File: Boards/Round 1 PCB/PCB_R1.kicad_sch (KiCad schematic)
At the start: 67 parts, among them J1 Screw_Terminal_01x12, J10 Screw_Terminal_01x03, J11 Screw_Terminal_01x12, J12 Screw_Terminal_01x03, J13 Screw_Terminal_01x03, J14 Screw_Terminal_01x03, J15 Screw_Terminal_01x03, J16 Screw_Terminal_01x03, J17 Screw_Terminal_01x03, J18 Screw_Terminal_01x03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

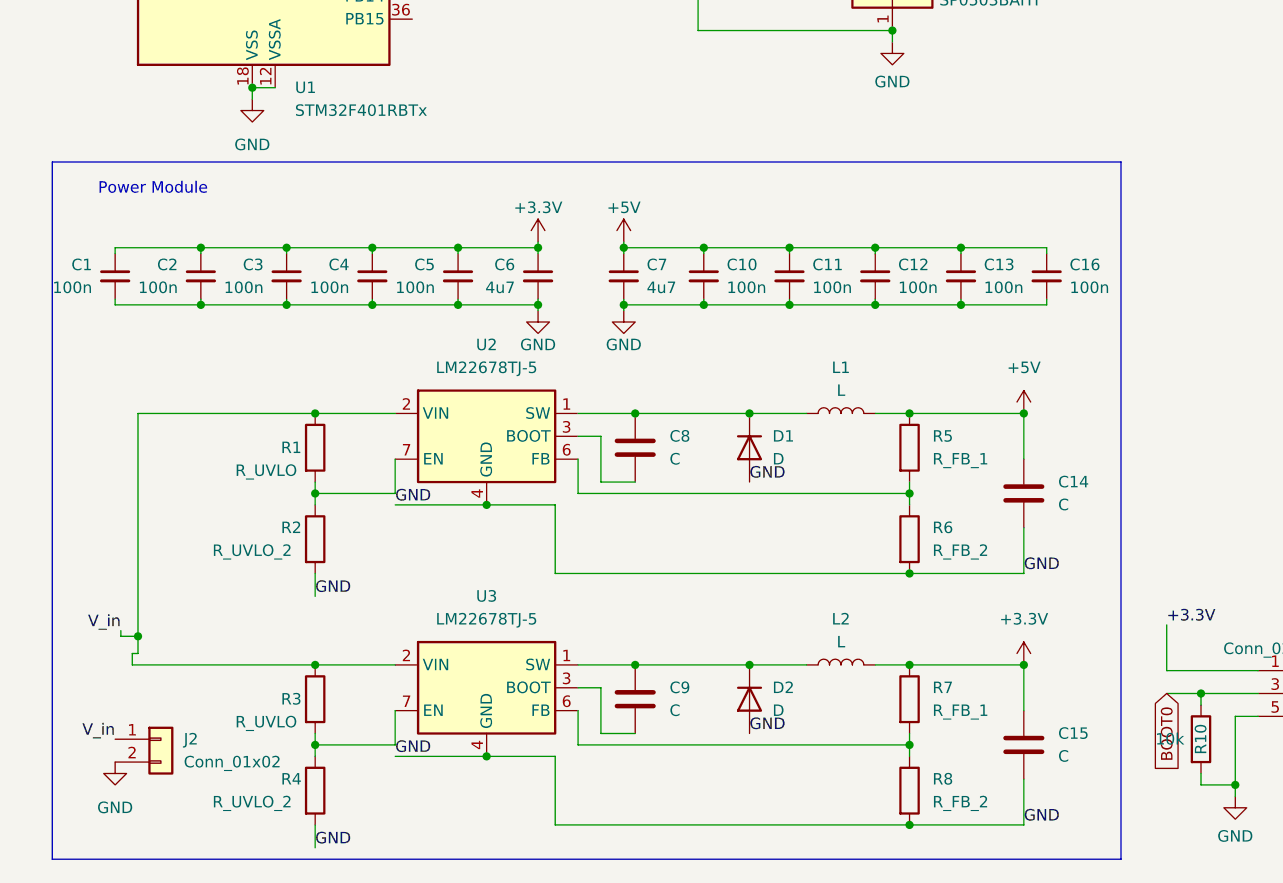
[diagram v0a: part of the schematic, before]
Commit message: Power System Update
added component values to the power system, and fixed ground nets
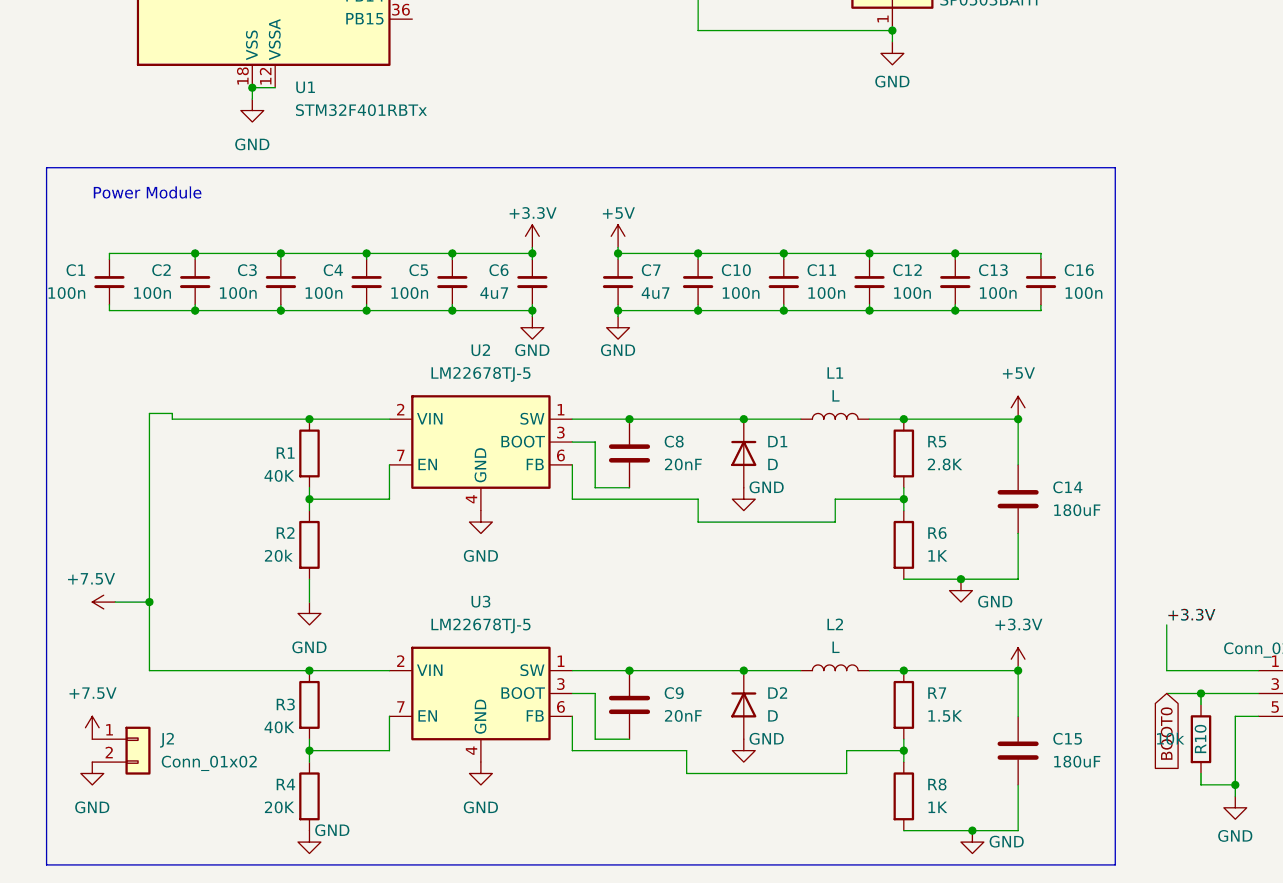
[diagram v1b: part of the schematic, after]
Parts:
- C14, C15: value C -> 180uF
- C8, C9: value C -> 20nF
- R1, R3: value R_UVLO -> 40K
- R2: value R_UVLO_2 -> 20k
- R4: value R_UVLO_2 -> 20K
- R5: value R_FB_1 -> 2.8K
- R6, R8: value R_FB_2 -> 1K
- R7: value R_FB_1 -> 1.5K
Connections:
- net V_in renamed +7.5V
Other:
- moved on the sheet: C1, C10, C11, C12, C13, C14, C15, C16, C2, C3, C4, C5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

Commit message: Inductor update
oops, I forgot the inductor values again
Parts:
- L1: value L -> 60uH
- L2: value L -> 2.2uH
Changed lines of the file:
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@@
       (effects (font (size 1.27 1.27)))
     )
-    (property "Value" "L" (at 100.33 172.72 90)
+    (property "Value" "2.2uH" (at 100.33 172.72 90)
       (effects (font (size 1.27 1.27)))
     )
@@
       (effects (font (size 1.27 1.27)))
     )
-    (property "Value" "L" (at 100.33 144.78 90)
-      (effects (font (size 1.27 1.27)))
-    )
+    (property "Value" "60uH" (at 100.33 144.78 90)
+      (effects (font (size 1.27 1.27)))
+    )

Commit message: Misc updates from 3/17/24
Touched up a few really minor things while I was doing the parts list
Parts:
- C17: value C -> 2.2uF
- D3: value SP0503BAHT -> SP0503BAHTG
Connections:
- net 3.3V_OUT is gone; now on net +3.3V: U1.13 (VREF+)
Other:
- note removed: "Gyroscope and Acceleromiter"

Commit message: r1 SMD footprint updates
changed component footprints on the board and schematic to use free smd components
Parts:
- C1, C10, C11, C12, C13, C16, C2, C3, C4, C5: footprint Capacitor_SMD:C_0402_1005Metric -> Capacitor_SMD:C_0805_2012Metric_Pad1.18x1.45mm_HandSolder
- C18, C6, C7: footprint Capacitor_SMD:C_0603_1608Metric -> Capacitor_SMD:C_0805_2012Metric_Pad1.18x1.45mm_HandSolder
- R10, R11, R17, R18, R19, R9: footprint Resistor_SMD:R_0603_1608Metric -> Resistor_SMD:R_0805_2012Metric_Pad1.20x1.40mm_HandSolder
- R12: footprint Resistor_SMD:R_0603_1608Metric -> Resistor_SMD:R_0805_2012Metric
- R6, R7, R8: footprint Resistor_SMD:R_1210_3225Metric_Pad1.30x2.65mm_HandSolder -> Resistor_SMD:R_0805_2012Metric_Pad1.20x1.40mm_HandSolder
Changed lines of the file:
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@@
       (effects (font (size 1.27 1.27)) (justify left))
     )
-    (property "Footprint" "Resistor_SMD:R_0603_1608Metric" (at 251.46 100.838 90)
+    (property "Footprint" "Resistor_SMD:R_0805_2012Metric_Pad1.20x1.40mm_HandSolder" (at 251.46 100.838 90)
       (effects (font (size 1.27 1.27)) hide)
     )
@@
       (effects (font (size 1.27 1.27)) (justify left))
     )
-    (property "Footprint" "Resistor_SMD:R_0603_1608Metric" (at 251.46 91.948 90)
+    (property "Footprint" "Resistor_SMD:R_0805_2012Metric_Pad1.20x1.40mm_HandSolder" (at 251.46 91.948 90)
       (effects (font (size 1.27 1.27)) hide)
     )
@@
       (effects (font (size 1.27 1.27)) (justify left))
     )
-    (property "Footprint" "Capacitor_SMD:C_0402_1005Metric" (at 85.09 132.08 0)
+    (property "Footprint" "Capacitor_SMD:C_0805_2012Metric_Pad1.18x1.45mm_HandSolder" (at 85.09 132.08 0)
       (effects (font (size 1.27 1.27)) hide)
     )
@@
       (effects (font (size 1.27 1.27)) (justify left))
     )
-    (property "Footprint" "Capacitor_SMD:C_0603_1608Metric" (at 154.0002 43.815 0)
+    (property "Footprint" "Capacitor_SMD:C_0805_2012Metric_Pad1.18x1.45mm_HandSolder" (at 154.0002 43.815 0)
       (effects (font (size 1.27 1.27)) hide)
     )
@@
       (effects (font (size 1.27 1.27)) (justify left))
     )
-    (property "Footprint" "Capacitor_SMD:C_0402_1005Metric" (at 38.735 132.08 0)
+    (property "Footprint" "Capacitor_SMD:C_0805_2012Metric_Pad1.18x1.45mm_HandSolder" (at 38.735 132.08 0)
       (effects (font (size 1.27 1.27)) hide)
     )
@@
       (effects (font (size 1.27 1.27)) (justify left))
     )
-    (property "Footprint" "Resistor_SMD:R_0603_1608Metric" (at 163.322 184.15 90)
+    (property "Footprint" "Resistor_SMD:R_0805_2012Metric_Pad1.20x1.40mm_HandSolder" (at 163.322 184.15 90)
       (effects (font (size 1.27 1.27)) hide)
     )
@@
       (effects (font (size 1.27 1.27)) (justify left))
     )
-    (property "Footprint" "Capacitor_SMD:C_0402_1005Metric" (at 113.665 132.08 0)
+    (property "Footprint" "Capacitor_SMD:C_0805_2012Metric_Pad1.18x1.45mm_HandSolder" (at 113.665 132.08 0)
       (effects (font (size 1.27 1.27)) hide)
     )
@@
       (effects (font (size 1.27 1.27)) (justify left))
     )
-    (property "Footprint" "Resistor_SMD:R_1210_3225Metric_Pad1.30x2.65mm_HandSolder" (at 106.172 161.29 90)
+    (property "Footprint" "Resistor_SMD:R_0805_2012Metric_Pad1.20x1.40mm_HandSolder" (at 106.172 161.29 90)
       (effects (font (size 1.27 1.27)) hide)
     )
@@
       (effects (font (size 1.27 1.27)) (justify left))
     )
-    (property "Footprint" "Capacitor_SMD:C_0603_1608Metric" (at 66.675 132.08 0)
+    (property "Footprint" "Capacitor_SMD:C_0805_2012Metric_Pad1.18x1.45mm_HandSolder" (at 66.675 132.08 0)
       (effects (font (size 1.27 1.27)) hide)
     )
@@
       (effects (font (size 1.27 1.27)) (justify left))
     )
-    (property "Footprint" "Capacitor_SMD:C_0603_1608Metric" (at 76.2 132.08 0)
+    (property "Footprint" "Capacitor_SMD:C_0805_2012Metric_Pad1.18x1.45mm_HandSolder" (at 76.2 132.08 0)
       (effects (font (size 1.27 1.27)) hide)
     )
@@
       (effects (font (size 1.27 1.27)) (justify left))
     )
-    (property "Footprint" "Capacitor_SMD:C_0402_1005Metric" (at 104.14 132.08 0)
+    (property "Footprint" "Capacitor_SMD:C_0805_2012Metric_Pad1.18x1.45mm_HandSolder" (at 104.14 132.08 0)
       (effects (font (size 1.27 1.27)) hide)
     )
@@
       (effects (font (size 1.27 1.27)) (justify left))
     )
-    (property "Footprint" "Capacitor_SMD:C_0402_1005Metric" (at 94.615 132.08 0)
+    (property "Footprint" "Capacitor_SMD:C_0805_2012Metric_Pad1.18x1.45mm_HandSolder" (at 94.615 132.08 0)
       (effects (font (size 1.27 1.27)) hide)
     )
@@
       (effects (font (size 1.27 1.27)) (justify left))
     )
-    (property "Footprint" "Resistor_SMD:R_0603_1608Metric" (at 139.192 182.88 90)
+    (property "Footprint" "Resistor_SMD:R_0805_2012Metric_Pad1.20x1.40mm_HandSolder" (at 139.192 182.88 90)
       (effects (font (size 1.27 1.27)) hide)
     )
@@
       (effects (font (size 1.27 1.27)) (justify left))
     )
-    (property "Footprint" "Resistor_SMD:R_0603_1608Metric" (at 102.362 64.77 90)
+    (property "Footprint" "Resistor_SMD:R_0805_2012Metric" (at 102.362 64.77 90)
       (effects (font (size 1.27 1.27)) hide)
     )
@@
       (effects (font (size 1.27 1.27)) (justify left))
     )
-    (property "Footprint" "Resistor_SMD:R_0603_1608Metric" (at 151.257 28.575 90)
+    (property "Footprint" "Resistor_SMD:R_0805_2012Metric_Pad1.20x1.40mm_HandSolder" (at 151.257 28.575 90)
       (effects (font (size 1.27 1.27)) hide)
     )
@@
       (effects (font (size 1.27 1.27)) (justify left))
     )
-    (property "Footprint" "Capacitor_SMD:C_0402_1005Metric" (at 48.26 132.08 0)
+    (property "Footprint" "Capacitor_SMD:C_0805_2012Metric_Pad1.18x1.45mm_HandSolder" (at 48.26 132.08 0)
       (effects (font (size 1.27 1.27)) hide)
     )
@@
       (effects (font (size 1.27 1.27)) (justify left))
     )
-    (property "Footprint" "Capacitor_SMD:C_0402_1005Metric" (at 123.19 132.08 0)
+    (property "Footprint" "Capacitor_SMD:C_0805_2012Metric_Pad1.18x1.45mm_HandSolder" (at 123.19 132.08 0)
       (effects (font (size 1.27 1.27)) hide)
     )
@@
       (effects (font (size 1.27 1.27)) (justify left))
     )
-    (property "Footprint" "Resistor_SMD:R_0603_1608Metric" (at 251.46 109.728 90)
+    (property "Footprint" "Resistor_SMD:R_0805_2012Metric_Pad1.20x1.40mm_HandSolder" (at 251.46 109.728 90)
       (effects (font (size 1.27 1.27)) hide)
     )
@@
       (effects (font (size 1.27 1.27)) (justify left))
     )
-    (property "Footprint" "Resistor_SMD:R_1210_3225Metric_Pad1.30x2.65mm_HandSolder" (at 106.172 189.23 90)
+    (property "Footprint" "Resistor_SMD:R_0805_2012Metric_Pad1.20x1.40mm_HandSolder" (at 106.172 189.23 90)
       (effects (font (size 1.27 1.27)) hide)
     )
@@
       (effects (font (size 1.27 1.27)) (justify left))
     )
-    (property "Footprint" "Capacitor_SMD:C_0402_1005Metric" (at 57.785 132.08 0)
+    (property "Footprint" "Capacitor_SMD:C_0805_2012Metric_Pad1.18x1.45mm_HandSolder" (at 57.785 132.08 0)
       (effects (font (size 1.27 1.27)) hide)
     )
@@
       (effects (font (size 1.27 1.27)) (justify left))
     )
-    (property "Footprint" "Resistor_SMD:R_1210_3225Metric_Pad1.30x2.65mm_HandSolder" (at 106.172 179.07 90)
+    (property "Footprint" "Resistor_SMD:R_0805_2012Metric_Pad1.20x1.40mm_HandSolder" (at 106.172 179.07 90)
       (effects (font (size 1.27 1.27)) hide)
     )
@@
       (effects (font (size 1.27 1.27)) (justify left))
     )
-    (property "Footprint" "Capacitor_SMD:C_0402_1005Metric" (at 19.685 132.08 0)
+    (property "Footprint" "Capacitor_SMD:C_0805_2012Metric_Pad1.18x1.45mm_HandSolder" (at 19.685 132.08 0)
       (effects (font (size 1.27 1.27)) hide)
     )
@@
       (effects (font (size 1.27 1.27)) (justify left))
     )
-    (property "Footprint" "Capacitor_SMD:C_0402_1005Metric" (at 29.21 132.08 0)
-      (effects (font (size 1.27 1.27)) hide)
-    )
+    (property "Footprint" "Capacitor_SMD:C_0805_2012Metric_Pad1.18x1.45mm_HandSolder" (at 29.21 132.08 0)
+      (effects (font (size 1.27 1.27)) hide)
+    )

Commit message: Resistor 0805 update
all resistors and capacitors are 0805 now, thanks Dad
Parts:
- C14, C15, C17, C8, C9: footprint Capacitor_SMD:C_1210_3225Metric_Pad1.33x2.70mm_HandSolder -> Capacitor_SMD:C_0805_2012Metric_Pad1.18x1.45mm_HandSolder
- R1, R2, R3, R4, R5: footprint Resistor_SMD:R_1210_3225Metric_Pad1.30x2.65mm_HandSolder -> Resistor_SMD:R_0805_2012Metric_Pad1.20x1.40mm_HandSolder
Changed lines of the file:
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@@
       (effects (font (size 1.27 1.27)) (justify left))
     )
-    (property "Footprint" "Capacitor_SMD:C_1210_3225Metric_Pad1.33x2.70mm_HandSolder" (at 78.4352 154.94 0)
+    (property "Footprint" "Capacitor_SMD:C_0805_2012Metric_Pad1.18x1.45mm_HandSolder" (at 78.4352 154.94 0)
       (effects (font (size 1.27 1.27)) hide)
     )
@@
       (effects (font (size 1.27 1.27)) (justify left))
     )
-    (property "Footprint" "Resistor_SMD:R_1210_3225Metric_Pad1.30x2.65mm_HandSolder" (at 40.132 179.07 90)
+    (property "Footprint" "Resistor_SMD:R_0805_2012Metric_Pad1.20x1.40mm_HandSolder" (at 40.132 179.07 90)
       (effects (font (size 1.27 1.27)) hide)
     )
@@
       (effects (font (size 1.27 1.27)) (justify left))
     )
-    (property "Footprint" "Resistor_SMD:R_1210_3225Metric_Pad1.30x2.65mm_HandSolder" (at 106.172 151.13 90)
+    (property "Footprint" "Resistor_SMD:R_0805_2012Metric_Pad1.20x1.40mm_HandSolder" (at 106.172 151.13 90)
       (effects (font (size 1.27 1.27)) hide)
     )
@@
       (effects (font (size 1.27 1.27)) (justify left))
     )
-    (property "Footprint" "Capacitor_SMD:C_1210_3225Metric_Pad1.33x2.70mm_HandSolder" (at 121.6152 160.02 0)
+    (property "Footprint" "Capacitor_SMD:C_0805_2012Metric_Pad1.18x1.45mm_HandSolder" (at 121.6152 160.02 0)
       (effects (font (size 1.27 1.27)) hide)
     )
@@
       (effects (font (size 1.27 1.27)) (justify left))
     )
-    (property "Footprint" "Resistor_SMD:R_1210_3225Metric_Pad1.30x2.65mm_HandSolder" (at 40.132 189.23 90)
+    (property "Footprint" "Resistor_SMD:R_0805_2012Metric_Pad1.20x1.40mm_HandSolder" (at 40.132 189.23 90)
       (effects (font (size 1.27 1.27)) hide)
     )
@@
       (effects (font (size 1.27 1.27)) (justify left))
     )
-    (property "Footprint" "Capacitor_SMD:C_1210_3225Metric_Pad1.33x2.70mm_HandSolder" (at 146.3802 67.945 0)
+    (property "Footprint" "Capacitor_SMD:C_0805_2012Metric_Pad1.18x1.45mm_HandSolder" (at 146.3802 67.945 0)
       (effects (font (size 1.27 1.27)) hide)
     )
@@
       (effects (font (size 1.27 1.27)) (justify left))
     )
-    (property "Footprint" "Resistor_SMD:R_1210_3225Metric_Pad1.30x2.65mm_HandSolder" (at 40.132 161.29 90)
+    (property "Footprint" "Resistor_SMD:R_0805_2012Metric_Pad1.20x1.40mm_HandSolder" (at 40.132 161.29 90)
       (effects (font (size 1.27 1.27)) hide)
     )
@@
       (effects (font (size 1.27 1.27)) (justify left))
     )
-    (property "Footprint" "Capacitor_SMD:C_1210_3225Metric_Pad1.33x2.70mm_HandSolder" (at 121.6152 187.96 0)
+    (property "Footprint" "Capacitor_SMD:C_0805_2012Metric_Pad1.18x1.45mm_HandSolder" (at 121.6152 187.96 0)
       (effects (font (size 1.27 1.27)) hide)
     )
@@
       (effects (font (size 1.27 1.27)) (justify left))
     )
-    (property "Footprint" "Capacitor_SMD:C_1210_3225Metric_Pad1.33x2.70mm_HandSolder" (at 78.4352 182.88 0)
+    (property "Footprint" "Capacitor_SMD:C_0805_2012Metric_Pad1.18x1.45mm_HandSolder" (at 78.4352 182.88 0)
       (effects (font (size 1.27 1.27)) hide)
     )
@@
       (effects (font (size 1.27 1.27)) (justify left))
     )
-    (property "Footprint" "Resistor_SMD:R_1210_3225Metric_Pad1.30x2.65mm_HandSolder" (at 40.132 151.13 90)
-      (effects (font (size 1.27 1.27)) hide)
-    )
+    (property "Footprint" "Resistor_SMD:R_0805_2012Metric_Pad1.20x1.40mm_HandSolder" (at 40.132 151.13 90)
+      (effects (font (size 1.27 1.27)) hide)
+    )
